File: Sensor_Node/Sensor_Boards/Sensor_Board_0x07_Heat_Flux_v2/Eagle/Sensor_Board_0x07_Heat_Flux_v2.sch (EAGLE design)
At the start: 14 parts, among them J1 M04_SMD_90, J4 ARDUINO_ISP, U2 ATMEGA328P_TQFP, Y1 8MHZ

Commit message: Work on heat flux sensor continued
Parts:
- removed R1: 10k, SparkFun-Passives:RESISTOR0805-RES
- removed S3: JS202011SCQN, myownthings:JS202011SCQN
- added C4, C5, C6, C8: 100n, eagle-ltspice:C
- added C7: 1u, eagle-ltspice:C
- added D1: LEDXLAMP_BAV99, Sensor_Board_0x07_Heat_Flux:LEDXLAMP_BAV99
- added IC1: HEATFLOW_MCP3911A0-E/SS, Sensor_Board_0x07_Heat_Flux:HEATFLOW_MCP3911A0-E/SS
- added IC2: 40XX_4066D, Sensor_Board_0x07_Heat_Flux:40XX_4066D
- added L1: HEATFLOW2_74279220601, Sensor_Board_0x07_Heat_Flux:HEATFLOW2_74279220601
- added PAD1, PAD2: WIREPADSMD1,27-254, wirepad:WIREPADSMD1,27-254
- added R4, R5: 10k, SparkFun-Passives:RESISTOR0805-RES
- added R6: 0, Sensor_Board_0x07_Heat_Flux:RESISTOR_R-EU_M0805
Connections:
- removed net DBG_ENABLE: R1.2, U2.PC3(ADC3)
- removed net GND: C2.2, C3.2, J1.4, J4.GND, LED1.C, S1.LEFT, S3.3, SV1.1, SV1.2, U2.AGND, U2.GND@3, U2.GND@5, Y1.2
- removed net N$3: R1.1, S3.2
- removed net VCC: C2.1, J1.1, J4.VCC, R2.2, S3.1, SV1.3, U2.AVCC, U2.VCC@4, U2.VCC@6
- new net AGND: C4.1, C5.2, C7.2, D1.A, D1.C, IC1.AGND, IC1.CH0-, IC1.CH1+, IC1.CH1-, IC1.REFIN-, IC2A.A, PAD2.P, R6.2
- new net AVCC: C5.1, IC1.AVDD, L1.P$2
- new net DGND: C2.2, C3.2, C6.2, C8.2, IC1.DGND, IC2C.A, IC2C.C, IC2D.A, IC2D.C, IC2P.VSS, J1.4, J4.GND, LED1.C, R6.1, S1.LEFT, SV1.1, SV1.2, U2.AGND, U2.GND@3, U2.GND@5, Y1.2
- new net DVCC: C2.1, C6.1, C8.1, IC1.DVDD, IC2P.VDD, J1.1, J4.VCC, L1.P$1, R2.2, R4.2, R5.2, SV1.3, U2.AVCC, U2.VCC@4, U2.VCC@6
- new net INPUT_EN: IC2B.C, U2.PC0(ADC0)
- new net INPUT_SHORT: IC2A.C, U2.PC1(ADC1)
- new net MCP_CLK: IC1.OSC1, U2.PB1(OC1A)
- new net MCP_CS: IC1./CS, R4.1, U2.PB0(ICP)
- new net MCP_DATA_RDY: IC1./DR, U2.PD3(INT1)
- new net MCP_RESET: IC1./RESET, R5.1, U2.PC2(ADC2)
- new net N$4: C4.2, IC1.REFIN+/OUT
- new net N$5: IC1.CH0+, IC2A.B, IC2B.B
- new net N$6: C7.1, D1.AC, IC2B.A, PAD1.P
- net MISO: now also IC1.SDO
- net MOSI: now also IC1.SDI
- net SCK: now also IC1.SCK
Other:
- note added: "2.0"
- note added: "Debug LED"
- note added: "Sensor Board - MCP3911"
- note removed: "1.0"
- note removed: "Debug Mode"
- note removed: "Sensor Board - Vorlage"
- moved on the sheet: LED1, R3

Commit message: Worked on heat flux board
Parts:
- added C10: 100n, eagle-ltspice:C
- added C9: 10n, eagle-ltspice:C
- added FB1, FB2: (no value), Adafruit_MAX31855 v2:MICROBUILDER_FERRITE_0805MP
- added IC4: ADAFRUIT_MAX31855, Adafruit_MAX31855 v2:ADAFRUIT_MAX31855
- added PAD10, PAD3, PAD4, PAD5, PAD6, PAD7, PAD8, PAD9: WIREPADSMD1,27-254, wirepad:WIREPADSMD1,27-254
- added R1, R7, R8: 10k, SparkFun-Passives:RESISTOR0805-RES
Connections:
- removed net SCL: U2.PC5(ADC5/SCL)
- removed net SDA: U2.PC4(ADC4/SDA)
- new net DS18B20_DATA_1: PAD4.P, R1.1, U2.PC3(ADC3)
- new net DS18B20_DATA_2: PAD7.P, R7.1, U2.PC2(ADC2)
- new net MAX_CS: IC4./CS, R8.1, U2.PC1(ADC1)
- new net N$3: FB1.P$1, PAD9.P
- new net N$7: FB2.P$1, PAD10.P
- new net N$8: C9.2, FB2.P$2, IC4.T-
- new net N$9: C9.1, FB1.P$2, IC4.T+
- net DGND: now also C10.2, IC4.GND, PAD5.P, PAD8.P
- net DVCC: now also C10.1, IC4.VCC, PAD3.P, PAD6.P, R1.2, R7.2, R8.2
- net INPUT_SHORT: now also U2.PD4(XCK/T0); no longer U2.PC1(ADC1)
- net MCP_CS: now also U2.PD5(T1); no longer U2.PB0(ICP)
- net MCP_RESET: now also U2.PB0(ICP); no longer U2.PC2(ADC2)
- net MISO: now also IC4.DO
- net SCK: now also IC4.SCK
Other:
- note added: "DS18B20"

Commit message: Continued on Heat Flux v2
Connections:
- net MCP_CS: now also U2.PB0(ICP); no longer U2.PD5(T1)
- net MCP_RESET: now also U2.PD5(T1); no longer U2.PB0(ICP)
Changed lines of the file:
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@@
 <?xml version="1.0" encoding="utf-8"?>
 <!DOCTYPE eagle SYSTEM "eagle.dtd">
-<eagle version="9.0.1">
+<eagle version="8.7.0">
 <drawing>
 <settings>
@@
 <setting verticaltext="up"/>
 </settings>
-<grid distance="0.1" unitdist="inch" unit="inch" style="lines" multiple="1" display="yes" altdistance="0.01" altunitdist="inch" altunit="inch"/>
+<grid distance="0.1" unitdist="inch" unit="inch" style="lines" multiple="1" display="no" altdistance="0.01" altunitdist="inch" altunit="inch"/>
 <layers>
 <layer number="1" name="Top" color="4" fill="1" visible="no" active="no"/>
@@
 </segment>
 <segment>
-<pinref part="U2" gate="U$1" pin="PB0(ICP)"/>
-<wire x1="99.06" y1="142.24" x2="101.6" y2="142.24" width="0.1524" layer="91"/>
-<label x="101.6" y="142.24" size="1.27" layer="95" xref="yes"/>
+<pinref part="U2" gate="U$1" pin="PD5(T1)"/>
+<wire x1="99.06" y1="149.86" x2="101.6" y2="149.86" width="0.1524" layer="91"/>
+<label x="101.6" y="149.86" size="1.27" layer="95" xref="yes"/>
 </segment>
 </net>
@@
 </segment>
 <segment>
-<pinref part="U2" gate="U$1" pin="PD5(T1)"/>
-<wire x1="99.06" y1="149.86" x2="101.6" y2="149.86" width="0.1524" layer="91"/>
-<label x="101.6" y="149.86" size="1.27" layer="95" xref="yes"/>
-</segment>
-</net>
+<pinref part="U2" gate="U$1" pin="PB0(ICP)"/>
+<wire x1="99.06" y1="142.24" x2="101.6" y2="142.24" width="0.1524" layer="91"/>
+<label x="101.6" y="142.24" size="1.27" layer="95" xref="yes"/>
+</segment>
+</net>

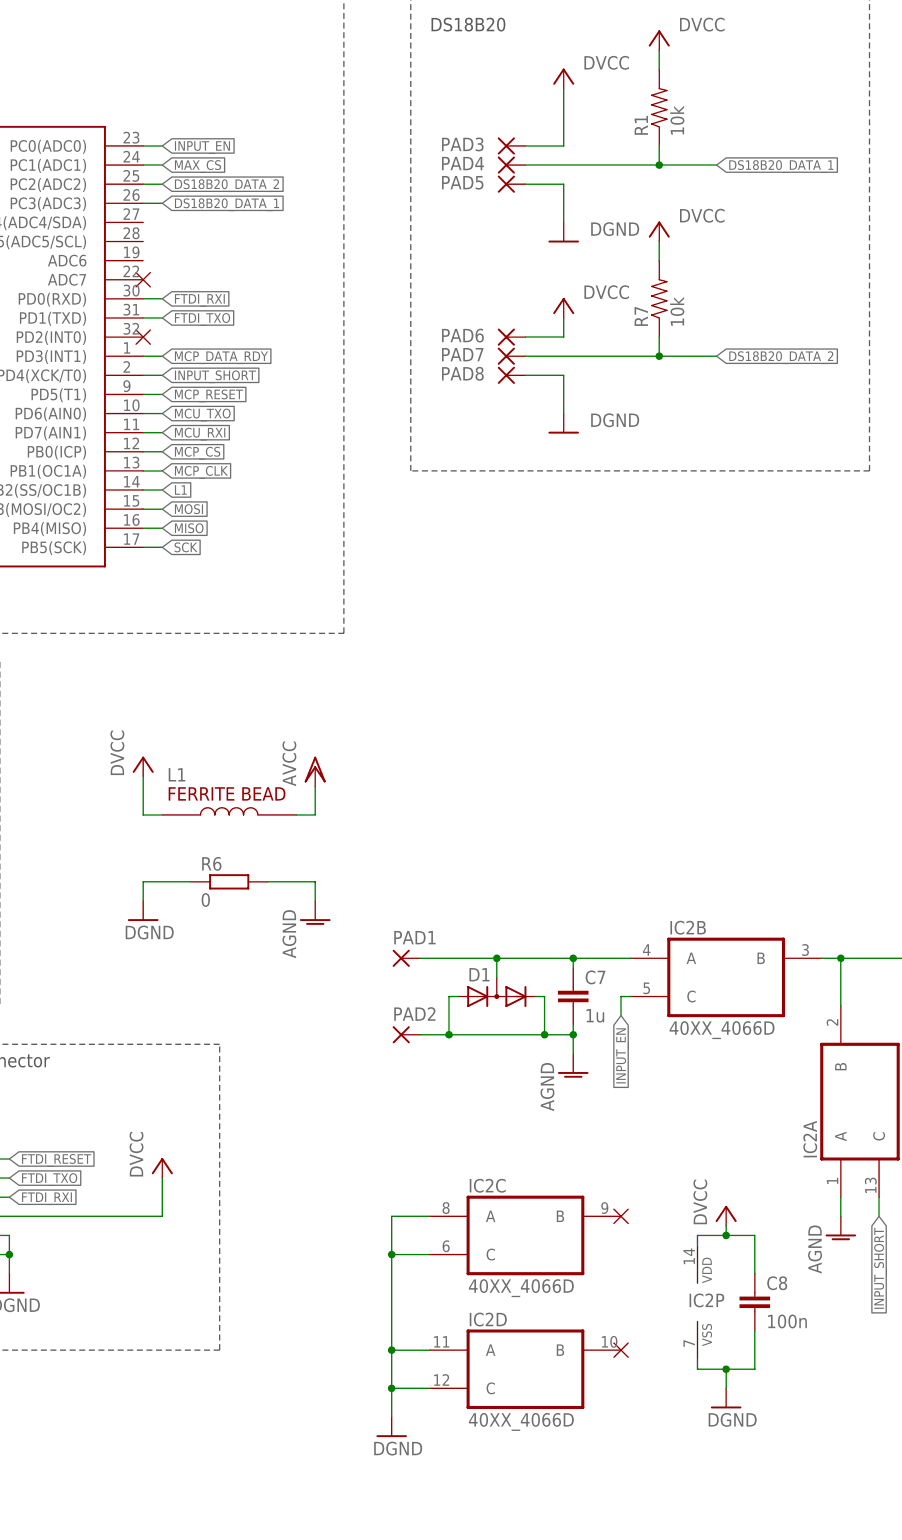
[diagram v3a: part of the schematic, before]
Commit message: Finished routing of heat flux v2
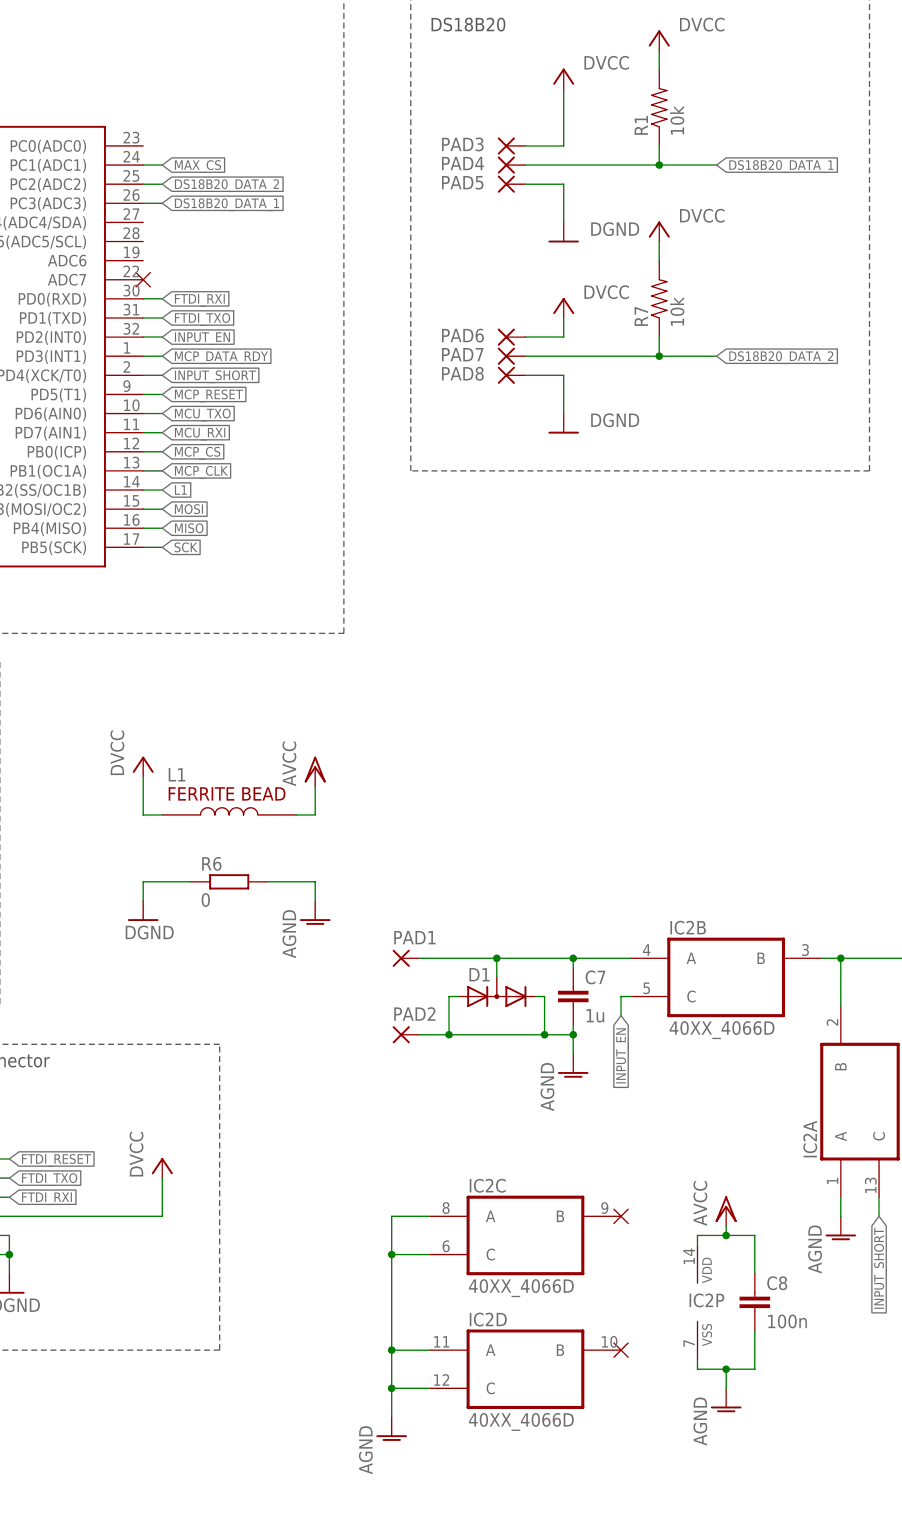
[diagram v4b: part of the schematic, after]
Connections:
- net AGND: now also C8.2, IC2C.A, IC2C.C, IC2D.A, IC2D.C, IC2P.VSS
- net AVCC: now also C8.1, IC2P.VDD
- net DGND: no longer C8.2, IC2C.A, IC2C.C, IC2D.A, IC2D.C, IC2P.VSS
- net DVCC: no longer C8.1, IC2P.VDD
- net INPUT_EN: now also U2.PD2(INT0); no longer U2.PC0(ADC0)
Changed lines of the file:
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@@
 <setting verticaltext="up"/>
 </settings>
-<grid distance="0.1" unitdist="inch" unit="inch" style="lines" multiple="1" display="no" altdistance="0.01" altunitdist="inch" altunit="inch"/>
+<grid distance="0.05" unitdist="inch" unit="inch" style="lines" multiple="1" display="yes" altdistance="0.01" altunitdist="inch" altunit="inch"/>
 <layers>
 <layer number="1" name="Top" color="4" fill="1" visible="no" active="no"/>
@@
 <part name="P+5" library="supply1" library_urn="urn:adsk.eagle:library:371" deviceset="VCC" device="" value="DVCC"/>
 <part name="U$4" library="myownthings" deviceset="N/C" device=""/>
-<part name="U$5" library="myownthings" deviceset="N/C" device=""/>
 <part name="J1" library="myownthings" deviceset="M04_SMD_90" device=""/>
 <part name="SV1" library="con-lstb" library_urn="urn:adsk.eagle:library:162" deviceset="MA06-1" device="" package3d_urn="urn:adsk.eagle:package:8340/1"/>
@@
 <part name="PAD2" library="wirepad" library_urn="urn:adsk.eagle:library:412" deviceset="WIREPAD" device="SMD1,27-254" package3d_urn="urn:adsk.eagle:package:30839/1"/>
 <part name="AGND5" library="supply1" library_urn="urn:adsk.eagle:library:371" deviceset="AGND" device=""/>
-<part name="GND6" library="SparkFun" deviceset="GND" device="" value="DGND"/>
 <part name="C8" library="eagle-ltspice" library_urn="urn:adsk.eagle:library:217" deviceset="C" device="" package3d_urn="urn:adsk.eagle:package:13265/1" value="100n"/>
-<part name="P+11" library="supply1" library_urn="urn:adsk.eagle:library:371" deviceset="VCC" device="" value="DVCC"/>
-<part name="GND7" library="SparkFun" deviceset="GND" device="" value="DGND"/>
 <part name="U$2" library="myownthings" deviceset="N/C" device=""/>
 <part name="U$6" library="myownthings" deviceset="N/C" device=""/>
@@
 <part name="R8" library="SparkFun-Passives" deviceset="RESISTOR" device="0805-RES" value="10k"/>
 <part name="P+18" library="supply1" library_urn="urn:adsk.eagle:library:371" deviceset="VCC" device="" value="DVCC"/>
+<part name="AGND7" library="supply1" library_urn="urn:adsk.eagle:library:371" deviceset="AGND" device=""/>
+<part name="AGND8" library="supply1" library_urn="urn:adsk.eagle:library:371" deviceset="AGND" device=""/>
+<part name="VDD4" library="supply1" library_urn="urn:adsk.eagle:library:371" deviceset="VDD" device="" value="AVCC"/>
 </parts>
 <sheets>
@@
 <instance part="P+5" gate="VCC" x="33.02" y="53.34"/>
 <instance part="U$4" gate="G$1" x="99.06" y="165.1"/>
-<instance part="U$5" gate="G$1" x="99.06" y="157.48"/>
 <instance part="J1" gate="G$1" x="15.24" y="45.72" rot="MR180"/>
 <instance part="SV1" gate="1" x="68.58" y="43.18"/>
@@
 </instance>
 <instance part="AGND5" gate="VR1" x="156.21" y="59.69"/>
-<instance part="GND6" gate="1" x="132.08" y="11.43"/>
 <instance part="C8" gate="G$1" x="180.34" y="30.48"/>
-<instance part="P+11" gate="VCC" x="176.53" y="41.91"/>
-<instance part="GND7" gate="1" x="176.53" y="15.24"/>
 <instance part="U$2" gate="G$1" x="162.56" y="40.64"/>
 <instance part="U$6" gate="G$1" x="162.56" y="22.86"/>
@@
 <attribute name="VALUE" x="284.48" y="175.26" size="1.778" layer="96"/>
 </instance>
+<instance part="AGND7" gate="VR1" x="132.08" y="11.43"/>
+<instance part="AGND8" gate="VR1" x="176.53" y="15.24"/>
+<instance part="VDD4" gate="G$1" x="176.53" y="41.91"/>
 </instances>
 <busses>
@@
 <pinref part="GND4" gate="1" pin="GND"/>
 <wire x1="285.75" y1="73.66" x2="285.75" y2="72.39" width="0.1524" layer="91"/>
-</segment>
-<segment>
-<pinref part="IC2" gate="C" pin="A"/>
-<wire x1="137.16" y1="40.64" x2="132.08" y2="40.64" width="0.1524" layer="91"/>
-<pinref part="IC2" gate="D" pin="C"/>
-<wire x1="132.08" y1="40.64" x2="132.08" y2="35.56" width="0.1524" layer="91"/>
-<wire x1="132.08" y1="35.56" x2="132.08" y2="22.86" width="0.1524" layer="91"/>
-<wire x1="132.08" y1="22.86" x2="132.08" y2="17.78" width="0.1524" layer="91"/>
-<wire x1="132.08" y1="17.78" x2="137.16" y2="17.78" width="0.1524" layer="91"/>
-<pinref part="IC2" gate="D" pin="A"/>
-<wire x1="137.16" y1="22.86" x2="132.08" y2="22.86" width="0.1524" layer="91"/>
-<junction x="132.08" y="22.86"/>
-<pinref part="IC2" gate="C" pin="C"/>
-<wire x1="137.16" y1="35.56" x2="132.08" y2="35.56" width="0.1524" layer="91"/>
-<junction x="132.08" y="35.56"/>
-<pinref part="GND6" gate="1" pin="GND"/>
-<wire x1="132.08" y1="13.97" x2="132.08" y2="17.78" width="0.1524" layer="91"/>
-<junction x="132.08" y="17.78"/>
-</segment>
-<segment>
-<pinref part="IC2" gate="P" pin="VSS"/>
-<wire x1="172.72" y1="21.59" x2="172.72" y2="20.32" width="0.1524" layer="91"/>
-<pinref part="C8" gate="G$1" pin="2"/>
-<wire x1="172.72" y1="20.32" x2="176.53" y2="20.32" width="0.1524" layer="91"/>
-<wire x1="176.53" y1="20.32" x2="180.34" y2="20.32" width="0.1524" layer="91"/>
-<wire x1="180.34" y1="20.32" x2="180.34" y2="25.4" width="0.1524" layer="91"/>
-<pinref part="GND7" gate="1" pin="GND"/>
-<wire x1="176.53" y1="17.78" x2="176.53" y2="20.32" width="0.1524" layer="91"/>
-<junction x="176.53" y="20.32"/>
 </segment>
 <segment>
@@
 <pinref part="C6" gate="G$1" pin="1"/>
 <wire x1="285.75" y1="85.09" x2="285.75" y2="81.28" width="0.1524" layer="91"/>
-</segment>
-<segment>
-<pinref part="IC2" gate="P" pin="VDD"/>
-<wire x1="172.72" y1="36.83" x2="172.72" y2="38.1" width="0.1524" layer="91"/>
-<wire x1="172.72" y1="38.1" x2="176.53" y2="38.1" width="0.1524" layer="91"/>
-<pinref part="C8" gate="G$1" pin="1"/>
-<wire x1="176.53" y1="38.1" x2="180.34" y2="38.1" width="0.1524" layer="91"/>
-<wire x1="180.34" y1="38.1" x2="180.34" y2="33.02" width="0.1524" layer="91"/>
-<pinref part="P+11" gate="VCC" pin="VCC"/>
-<wire x1="176.53" y1="38.1" x2="176.53" y2="39.37" width="0.1524" layer="91"/>
-<junction x="176.53" y="38.1"/>
 </segment>
 <segment>
@@
 <wire x1="121.92" y1="85.09" x2="115.57" y2="85.09" width="0.1524" layer="91"/>
 </segment>
+<segment>
+<pinref part="IC2" gate="C" pin="A"/>
+<wire x1="137.16" y1="40.64" x2="132.08" y2="40.64" width="0.1524" layer="91"/>
+<pinref part="IC2" gate="D" pin="C"/>
+<wire x1="132.08" y1="40.64" x2="132.08" y2="35.56" width="0.1524" layer="91"/>
+<wire x1="132.08" y1="35.56" x2="132.08" y2="22.86" width="0.1524" layer="91"/>
+<wire x1="132.08" y1="22.86" x2="132.08" y2="17.78" width="0.1524" layer="91"/>
+<wire x1="132.08" y1="17.78" x2="137.16" y2="17.78" width="0.1524" layer="91"/>
+<pinref part="IC2" gate="D" pin="A"/>
+<wire x1="137.16" y1="22.86" x2="132.08" y2="22.86" width="0.1524" layer="91"/>
+<junction x="132.08" y="22.86"/>
+<pinref part="IC2" gate="C" pin="C"/>
+<wire x1="137.16" y1="35.56" x2="132.08" y2="35.56" width="0.1524" layer="91"/>
+<junction x="132.08" y="35.56"/>
+<wire x1="132.08" y1="13.97" x2="132.08" y2="17.78" width="0.1524" layer="91"/>
+<junction x="132.08" y="17.78"/>
+<pinref part="AGND7" gate="VR1" pin="AGND"/>
+</segment>
+<segment>
+<pinref part="IC2" gate="P" pin="VSS"/>
+<wire x1="172.72" y1="21.59" x2="172.72" y2="20.32" width="0.1524" layer="91"/>
+<pinref part="C8" gate="G$1" pin="2"/>
+<wire x1="172.72" y1="20.32" x2="176.53" y2="20.32" width="0.1524" layer="91"/>
+<wire x1="176.53" y1="20.32" x2="180.34" y2="20.32" width="0.1524" layer="91"/>
+<wire x1="180.34" y1="20.32" x2="180.34" y2="25.4" width="0.1524" layer="91"/>
+<wire x1="176.53" y1="17.78" x2="176.53" y2="20.32" width="0.1524" layer="91"/>
+<junction x="176.53" y="20.32"/>
+<pinref part="AGND8" gate="VR1" pin="AGND"/>
+</segment>
 </net>
 <net name="AVCC" class="0">
@@
 <wire x1="121.92" y1="97.79" x2="121.92" y2="93.98" width="0.1524" layer="91"/>
 <wire x1="121.92" y1="93.98" x2="119.38" y2="93.98" width="0.1524" layer="91"/>
+</segment>
+<segment>
+<pinref part="IC2" gate="P" pin="VDD"/>
+<wire x1="172.72" y1="36.83" x2="172.72" y2="38.1" width="0.1524" layer="91"/>
+<wire x1="172.72" y1="38.1" x2="176.53" y2="38.1" width="0.1524" layer="91"/>
+<pinref part="C8" gate="G$1" pin="1"/>
+<wire x1="176.53" y1="38.1" x2="180.34" y2="38.1" width="0.1524" layer="91"/>
+<wire x1="180.34" y1="38.1" x2="180.34" y2="33.02" width="0.1524" layer="91"/>
+<wire x1="176.53" y1="38.1" x2="176.53" y2="39.37" width="0.1524" layer="91"/>
+<junction x="176.53" y="38.1"/>
+<pinref part="VDD4" gate="G$1" pin="VDD"/>
 </segment>
 </net>
@@
 </segment>
 <segment>
-<pinref part="U2" gate="U$1" pin="PC0(ADC0)"/>
-<wire x1="99.06" y1="182.88" x2="101.6" y2="182.88" width="0.1524" layer="91"/>
-<label x="101.6" y="182.88" size="1.27" layer="95" xref="yes"/>
-</segment>
-</net>
+<pinref part="U2" gate="U$1" pin="PD2(INT0)"/>
+<wire x1="99.06" y1="157.48" x2="101.6" y2="157.48" width="0.1524" layer="91"/>
+<label x="101.6" y="157.48" size="1.27" layer="95" xref="yes"/>
+</segment>
+</net>

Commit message: Weiterarbeit Heat Flux
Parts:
- renumbered LED1 to LED
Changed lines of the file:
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@@
 <?xml version="1.0" encoding="utf-8"?>
 <!DOCTYPE eagle SYSTEM "eagle.dtd">
-<eagle version="8.7.0">
+<eagle version="9.0.1">
 <drawing>
 <settings>
@@
 <setting verticaltext="up"/>
 </settings>
-<grid distance="0.05" unitdist="inch" unit="inch" style="lines" multiple="1" display="yes" altdistance="0.01" altunitdist="inch" altunit="inch"/>
+<grid distance="0.1" unitdist="inch" unit="inch" style="lines" multiple="1" display="no" altdistance="0.01" altunitdist="inch" altunit="inch"/>
 <layers>
 <layer number="1" name="Top" color="4" fill="1" visible="no" active="no"/>
@@
 <part name="C3" library="eagle-ltspice" library_urn="urn:adsk.eagle:library:217" deviceset="C" device="" package3d_urn="urn:adsk.eagle:package:13265/1" value="100n"/>
 <part name="GND5" library="SparkFun-Aesthetics" deviceset="GND" device="" value="DGND"/>
-<part name="LED1" library="led" library_urn="urn:adsk.eagle:library:259" deviceset="LED" device="SML0805" package3d_urn="urn:adsk.eagle:package:15830/1" value="Red"/>
+<part name="LED" library="led" library_urn="urn:adsk.eagle:library:259" deviceset="LED" device="SML0805" package3d_urn="urn:adsk.eagle:package:15830/1" value="Red"/>
 <part name="R3" library="SparkFun-Passives" deviceset="RESISTOR" device="0805-RES" value="330"/>
 <part name="GND20" library="SparkFun-Aesthetics" deviceset="GND" device="" value="DGND"/>
@@
 <instance part="C3" gate="G$1" x="33.02" y="149.86"/>
 <instance part="GND5" gate="1" x="40.64" y="96.52"/>
-<instance part="LED1" gate="G$1" x="71.12" y="83.82"/>
+<instance part="LED" gate="G$1" x="71.12" y="83.82"/>
 <instance part="R3" gate="G$1" x="71.12" y="96.52" rot="R90"/>
 <instance part="GND20" gate="1" x="71.12" y="73.66"/>
@@
 <segment>
 <pinref part="GND20" gate="1" pin="GND"/>
-<pinref part="LED1" gate="G$1" pin="C"/>
+<pinref part="LED" gate="G$1" pin="C"/>
 <wire x1="71.12" y1="76.2" x2="71.12" y2="78.74" width="0.1524" layer="91"/>
 </segment>
@@
 <net name="N$30" class="0">
 <segment>
-<pinref part="LED1" gate="G$1" pin="A"/>
+<pinref part="LED" gate="G$1" pin="A"/>
 <pinref part="R3" gate="G$1" pin="1"/>
 <wire x1="71.12" y1="86.36" x2="71.12" y2="91.44" width="0.1524" layer="91"/>
